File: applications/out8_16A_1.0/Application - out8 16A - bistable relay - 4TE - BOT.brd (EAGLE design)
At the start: 86.3 x 67.3 mm, 30 parts, among them IC1 ULN2803, IC2 ULN2803, K1 HFE20-1-024-1HD504, K2 HFE20-1-024-1HD504, K3 HFE20-1-024-1HD504, K4 HFE20-1-024-1HD504, K5 HFE20-1-024-1HD504, K6 HFE20-1-024-1HD504, K7 HFE20-1-024-1HD504, K8 HFE20-1-024-1HD504

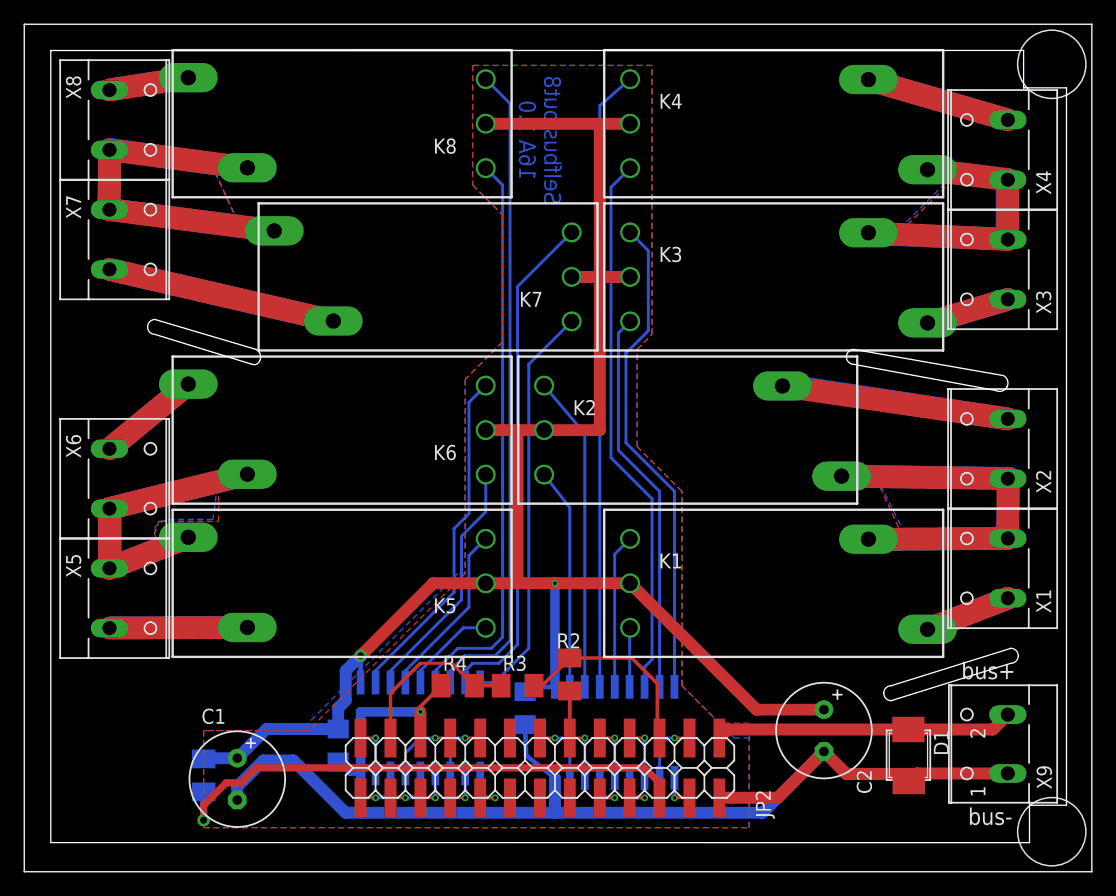
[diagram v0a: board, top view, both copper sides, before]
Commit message: renamed out8-V2.1 --> Application - out8 16A - bistable relay - 4TE - BOT
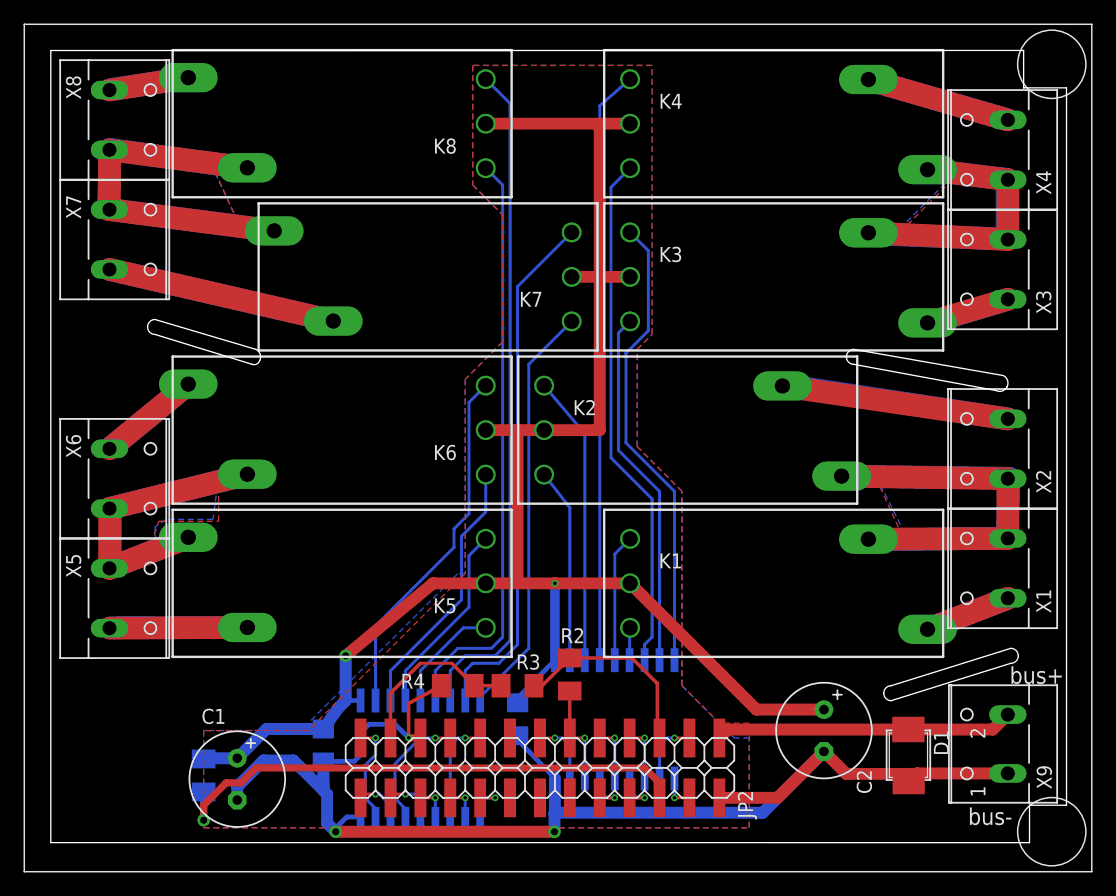
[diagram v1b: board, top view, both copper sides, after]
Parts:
- IC1, IC2: device uln-udn:SOP18 -> uln-udn:SO18W
- moved IC2 3.24 mm to (33.7, 9.59)
- moved C4 1.26 mm to (25.4, 10.8)
- moved C3 1.14 mm to (41.9, 13.0)
- moved IC1 0.90 mm to (50.2, 13.0)
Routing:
- net IO12: track 4.28 -> 8.92 mm
- net IO10: track 6.08 -> 10.7 mm
- net GND: track 114.6 -> 119.2 mm, vias 1 -> 3
- net IO16: track 5.18 -> 9.04 mm
- net O4: track 18.8 -> 16.5 mm
- net O1: track 13.1 -> 10.8 mm
- net O2: track 5.04 -> 2.76 mm
- net O8: track 46.5 -> 44.2 mm
- net O7: track 52.8 -> 50.5 mm
- net O6: track 32.9 -> 30.6 mm
- net O5: track 41.8 -> 39.5 mm
- net O3: track 26.9 -> 24.6 mm
- net VDD: track 151.5 -> 149.9 mm
- net O16: track 55.7 -> 57.2 mm
- net O15: track 48.3 -> 49.9 mm
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- added copper zone on layer 1, net GND
- added copper zone on layer 16, net GND
- removed copper zone on layer 16, net N$10
- removed copper zone on layer 1, net N$6
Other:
- board text added: "Selfbus out8 16A 2.1"
- board text removed: "Selfbus out8 16A 1.0"

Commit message: updated Application - out8 16A - bistable relay - 4TE - BOT - V2.2; added SJ2 for use with addon - energy storage; opütimized silkscreen and relaypositions
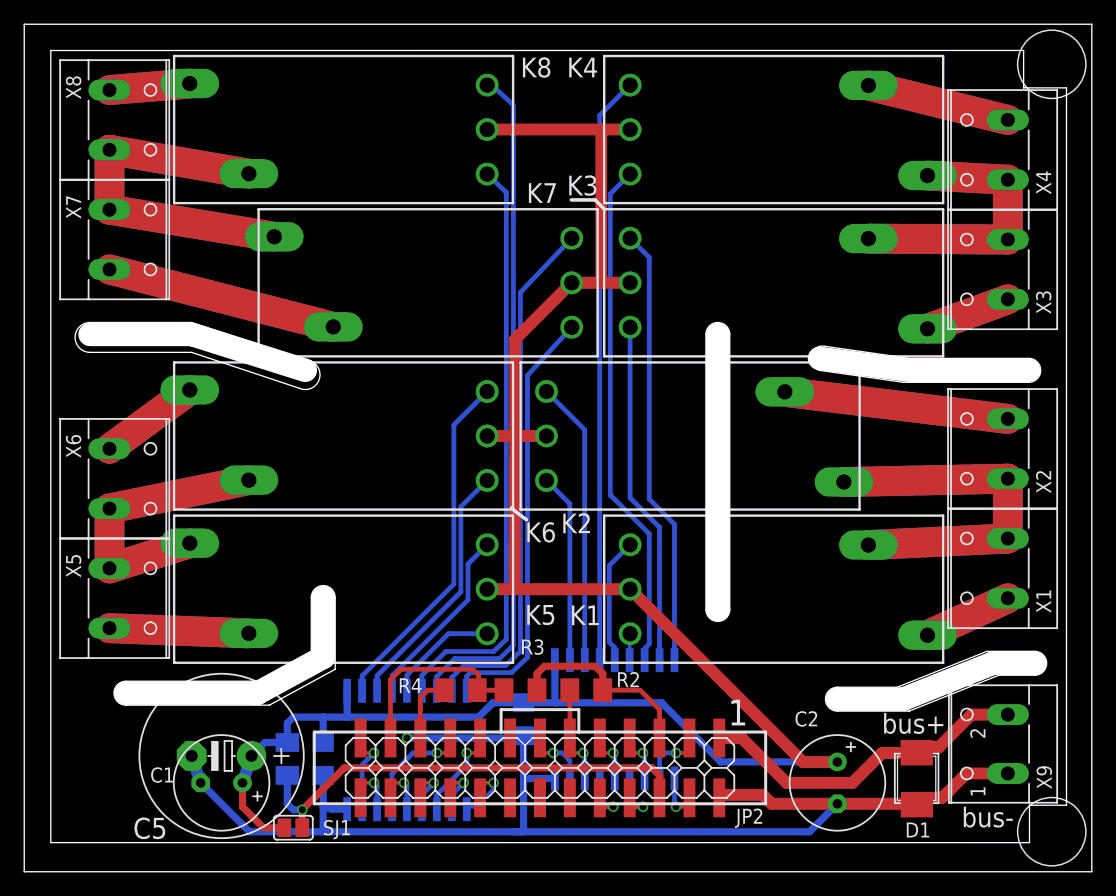
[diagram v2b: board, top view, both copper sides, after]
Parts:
- added C5: optional RM5,0, rcl:E5-13
- added SJ1: (no value), jumper:SJ
- C1, C2: value (none) -> 330µF/35V
- D1: value (none) -> SMAJ40CA
- K1, K2, K3, K4, K5, K6, K7, K8: value HFE20-1-024-1HD504 -> HFE20-1
- moved R1 7.25 mm to (22.4, 9.65)
- moved C2 4.59 mm to (69.1, 7.62)
- moved D1 2.09 mm to (75.9, 7.87)
- moved R2 1.93 mm to (47.8, 15.5), turned to 0 degrees
- moved IC2 1.41 mm to (32.5, 10.4)
- moved C1 1.37 mm to (16.8, 7.62), turned to 180 degrees
- moved C4 1.14 mm to (25.4, 9.65)
- moved K2 0.54 mm to (57.0, 37.1)
- moved K5 0.52 mm to (26.7, 24.1)
- moved K6 0.52 mm to (26.7, 37.1)
- moved K8 0.52 mm to (26.7, 63.1)
- moved C3 0.51 mm to (42.4, 13.0)
- moved K1 0.50 mm to (64.1, 24.1)
- moved K3 0.50 mm to (64.1, 50.1)
- moved K4 0.50 mm to (64.1, 63.1)
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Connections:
- net VCC_3V3 renamed +3V3
- net EIB_DC: now also SJ1.1
- net GND: now also C5.-
- net VDD: now also C5.+, SJ1.2
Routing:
- net VDD: track 149.9 -> 170.5 mm, vias 2 -> 0
- net EIB_DC: track 46.2 -> 40.0 mm
- net EIB+: track 25.3 -> 28.5 mm
- net O5: track 39.5 -> 37.4 mm
- net IO15: track 3.06 -> 5.07 mm
- net IO14: track 3.06 -> 5.07 mm
- net IO13: track 4.33 -> 6.10 mm
- net APP_SEL: track 15.0 -> 16.6 mm
- net IO5: track 2.91 -> 4.36 mm
- net IO2: track 3.81 -> 5.23 mm
- net IO7: track 3.81 -> 5.23 mm
- net GND: track 119.2 -> 120.6 mm, vias 3 -> 1
- net O6: track 30.6 -> 29.3 mm
- net IO12: track 8.92 -> 7.61 mm
- net O13: track 35.4 -> 36.6 mm
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- removed copper zone on layer 1, net GND
- removed copper zone on layer 16, net GND
- removed copper zone on layer 1, net K12
- removed copper zone on layer 16, net K12
- removed copper zone on layer 1, net K34
- removed copper zone on layer 16, net K34
- removed copper zone on layer 1, net K56
- removed copper zone on layer 16, net K56
- removed copper zone on layer 1, net K78
- removed copper zone on layer 16, net K78
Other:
- board text added: "1"
- board text added: "K1"
- board text added: "K2"
- board text added: "K3"
- board text added: "K4"
- board text added: "K5"
- board text added: "K6"
- board text added: "K7"
- board text added: "K8"
- board text added: "www.selfbus.org Schaltaktor out8 16A V2.2"
- board text removed: "Selfbus out8 16A 2.1"

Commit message: C5 entfernt Polygone eingefügt
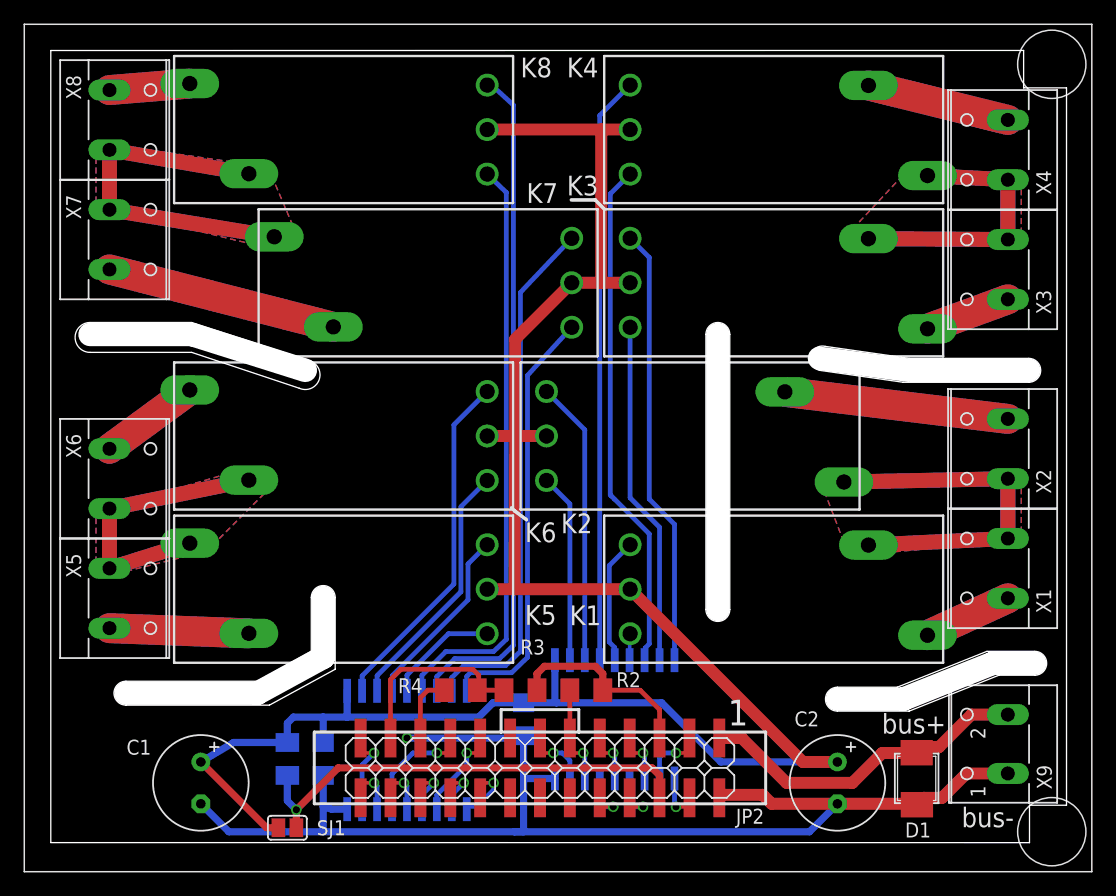
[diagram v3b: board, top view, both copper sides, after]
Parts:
- removed C5: optional RM5,0, rcl:E5-13
- moved C1 1.76 mm to (15.0, 7.62), turned to 270 degrees
- moved SJ1 0.51 mm to (22.4, 3.81)
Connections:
- net GND: no longer C5.-
- net VDD: no longer C5.+
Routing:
- net VDD: track 170.5 -> 175.0 mm
- net GND: track 120.6 -> 117.4 mm
- added copper zone on layer 1, net K12
- added copper zone on layer 16, net K12
- added copper zone on layer 1, net K34
- added copper zone on layer 16, net K34
- added copper zone on layer 1, net K56
- added copper zone on layer 16, net K56
- added copper zone on layer 1, net K78
- added copper zone on layer 16, net K78
